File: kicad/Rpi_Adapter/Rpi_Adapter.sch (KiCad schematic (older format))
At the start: 3 parts, among them P1 CONN_02X20, P2 CONN_01X08

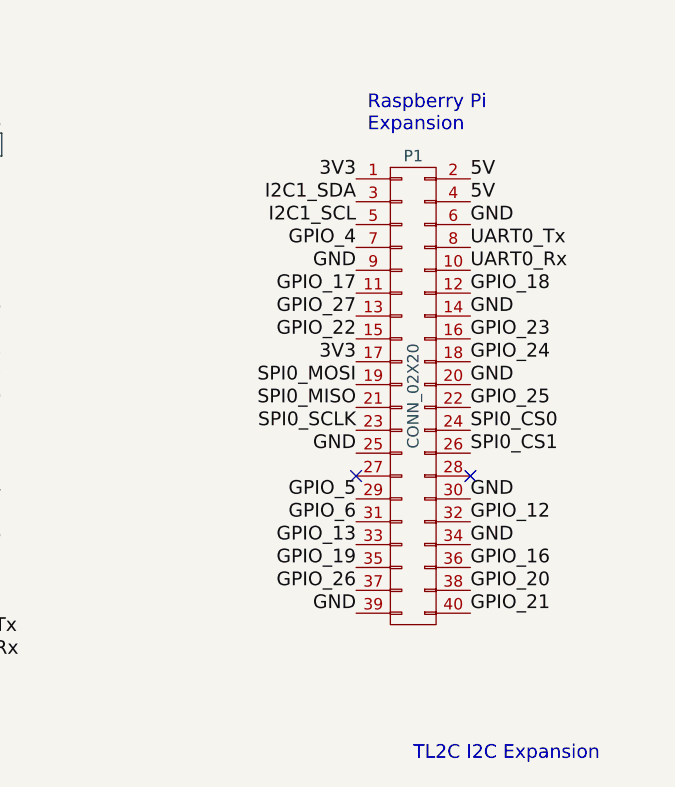
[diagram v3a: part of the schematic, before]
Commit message: Radically reduced the size of the board
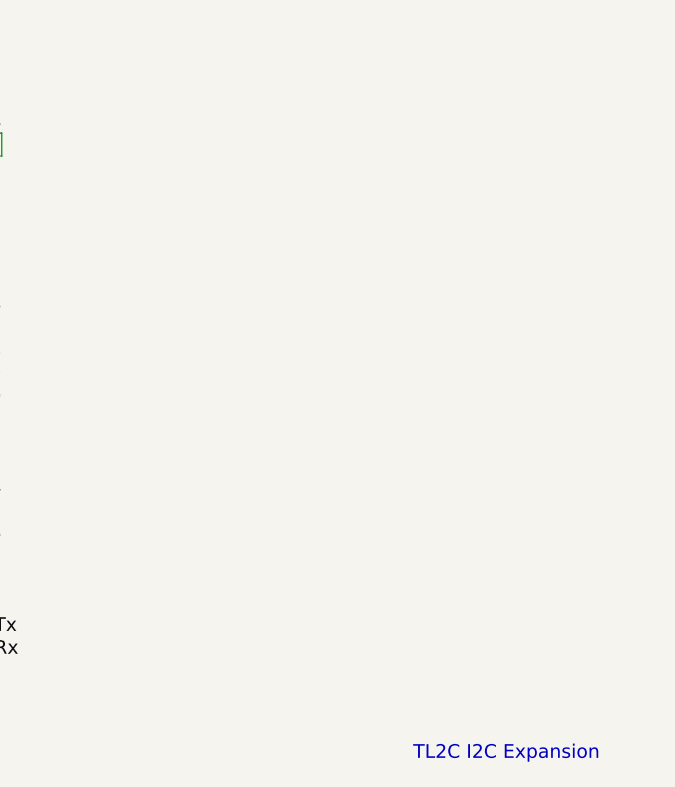
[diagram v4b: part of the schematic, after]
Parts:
- removed P1: CONN_02X20, Pin_Headers:Pin_Header_Straight_2x20_Pitch2.54mm, symbol CONN_02X20
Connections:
- no-connect marks 2 -> 0
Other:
- note removed: "Raspberry Pi\nExpansion"
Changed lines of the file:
@@
 	1    0    0    -1
 $EndComp
-$Comp
-L CONN_02X20 P1
-U 1 1 59479B40
-P 5850 2650
-F 0 "P1" H 5850 3700 50  0000 C CNN
-F 1 "CONN_02X20" V 5850 2650 50  0000 C CNN
-F 2 "Pin_Headers:Pin_Header_Straight_2x20_Pitch2.54mm" H 5850 1700 60  0001 C CNN
-F 3 "" H 5850 1700 60  0000 C CNN
-	1    5850 2650
-	1    0    0    -1
-$EndComp
-Text Label 5600 1700 2    60   ~ 0
-3V3
-Text Label 6100 1700 0    60   ~ 0
-5V
-Text Label 6100 1800 0    60   ~ 0
-5V
-Text Label 5600 2500 2    60   ~ 0
-3V3
-Text Label 5600 2000 2    60   ~ 0
-GPIO_4
-Text Label 5600 3100 2    60   ~ 0
-GPIO_5
-Text Label 5600 3200 2    60   ~ 0
-GPIO_6
-Text Label 6100 3200 0    60   ~ 0
-GPIO_12
-Text Label 5600 3300 2    60   ~ 0
-GPIO_13
-Text Label 6100 3400 0    60   ~ 0
-GPIO_16
-Text Label 5600 2200 2    60   ~ 0
-GPIO_17
-Text Label 6100 2200 0    60   ~ 0
-GPIO_18
-Text Label 5600 3400 2    60   ~ 0
-GPIO_19
-Text Label 6100 3500 0    60   ~ 0
-GPIO_20
-Text Label 6100 3600 0    60   ~ 0
-GPIO_21
-Text Label 5600 2400 2    60   ~ 0
-GPIO_22
-Text Label 6100 2400 0    60   ~ 0
-GPIO_23
-Text Label 6100 2500 0    60   ~ 0
-GPIO_24
-Text Label 6100 2700 0    60   ~ 0
-GPIO_25
-Text Label 5600 3500 2    60   ~ 0
-GPIO_26
-Text Label 5600 2300 2    60   ~ 0
-GPIO_27
-Text Label 6100 2000 0    60   ~ 0
-UART0_Tx
-Text Label 6100 2100 0    60   ~ 0
-UART0_Rx
-Text Label 5600 2600 2    60   ~ 0
-SPI0_MOSI
-Text Label 5600 2700 2    60   ~ 0
-SPI0_MISO
-Text Label 5600 2800 2    60   ~ 0
-SPI0_SCLK
-Text Label 6100 2800 0    60   ~ 0
-SPI0_CS0
-Text Label 6100 2900 0    60   ~ 0
-SPI0_CS1
-Text Label 5600 1800 2    60   ~ 0
-I2C1_SDA
-Text Label 5600 1900 2    60   ~ 0
-I2C1_SCL
-Text Label 6100 1900 0    60   ~ 0
-GND
-Text Label 5600 2100 2    60   ~ 0
-GND
-Text Label 6100 2300 0    60   ~ 0
-GND
-Text Label 6100 2600 0    60   ~ 0
-GND
-Text Label 5600 2900 2    60   ~ 0
-GND
-Text Label 6100 3100 0    60   ~ 0
-GND
-Text Label 6100 3300 0    60   ~ 0
-GND
-Text Label 5600 3600 2    60   ~ 0
-GND
-NoConn ~ 5600 3000
-NoConn ~ 6100 3000
 Text Label 4050 1500 2    60   ~ 0
 3V3
@@
 Text Label 6500 5200 2    60   ~ 0
 GPIO_5
-Text Notes 5650 1500 0    60   ~ 0
-Raspberry Pi\nExpansion
 Text Notes 5850 4250 0    60   ~ 0
 TL2C I2C Expansion
